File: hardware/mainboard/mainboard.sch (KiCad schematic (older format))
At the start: 3 parts, among them J1 top header, J4 bottom header, J5 almost bottom header

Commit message: First pass layout & component selection for mainboard
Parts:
- removed J1: top header, MF_Connectors:MF_Connectors-PTH_2.54MM_01X14, symbol Connector_Generic:Conn_01x14
- added MH1: M3, MountingHole:MountingHole_3.2mm_M3_Pad_Via, symbol Mechanical:MountingHole_Pad
- J4: value bottom header -> left header; footprint MF_Connectors:MF_Connectors-PTH_2.54MM_01X24 -> Connector_PinHeader_2.54mm:PinHeader_1x20_P2.54mm_Vertical; symbol Connector_Generic:Conn_01x24 -> Connector_Generic:Conn_01x20; finalized (none) -> yes; mpn (none) -> MF-CON-2.54mm-01x20
- J5: value almost bottom header -> right header; footprint MF_Connectors:MF_Connectors-PTH_2.54MM_01X14 -> Connector_PinHeader_2.54mm:PinHeader_1x20_P2.54mm_Vertical; symbol Connector_Generic:Conn_01x14 -> Connector_Generic:Conn_01x20; finalized (none) -> yes; mpn (none) -> MF-CON-2.54mm-01x20
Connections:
- net +12v-raw: now also J5.18 (Pin_18), J5.19 (Pin_19)
- net +3.3VA: now also J4.17 (Pin_17)
- net +3V3: now also J5.17 (Pin_17)
- net -12v-raw: now also J4.18 (Pin_18), J4.19 (Pin_19)
- net GND: now also J4.20 (Pin_20), J5.1 (Pin_1), J5.20 (Pin_20), MH1.1; no longer J4.12 (Pin_12), J4.13 (Pin_13), J4.24 (Pin_24), J5.7 (Pin_7), J5.8 (Pin_8)
- net castor_mix_out: now also J4.3 (Pin_3); no longer J5.12 (Pin_12)
- net castor_pwm_mix_in: now also J4.5 (Pin_5); no longer J4.20 (Pin_20)
- net castor_pwm_out: now also J4.8 (Pin_8); no longer J5.13 (Pin_13)
- net castor_ramp_mix_in: now also J4.6 (Pin_6); no longer J4.21 (Pin_21)
- net castor_ramp_out: now also J4.9 (Pin_9); no longer J4.23 (Pin_23)
- net castor_sub_mix_in: now also J4.4 (Pin_4); no longer J5.14 (Pin_14)
- net castor_sub_out: now also J4.7 (Pin_7); no longer J4.22 (Pin_22)
- net cv_a_jack: now also J5.8 (Pin_8); no longer J5.1 (Pin_1)
- net cv_a_pot: now also J5.14 (Pin_14); no longer J5.3 (Pin_3)
- net cv_b_jack: now also J5.7 (Pin_7); no longer J5.2 (Pin_2)
- net cv_b_pot: now also J5.13 (Pin_13); no longer J4.8 (Pin_8)
- net dotstar_clk: now also J5.16 (Pin_16)
- net dotstar_data: now also J5.15 (Pin_15)
- net duty_a_jack: now also J5.5 (Pin_5); no longer J4.2 (Pin_2)
- net duty_a_pot: now also J5.11 (Pin_11); no longer J4.7 (Pin_7)
- net duty_b_jack: now also J5.9 (Pin_9); no longer J4.3 (Pin_3)
- net duty_b_pot: now also J5.10 (Pin_10); no longer J4.5 (Pin_5)
- net mix_out: now also J5.2 (Pin_2); no longer J5.5 (Pin_5)
- net mix_pot_in: now also J5.3 (Pin_3); no longer J5.4 (Pin_4)
- net mix_pot_out: now also J5.4 (Pin_4); no longer J5.6 (Pin_6)
- net phase_jack: now also J5.6 (Pin_6); no longer J4.4 (Pin_4)
- net phase_pot: now also J5.12 (Pin_12); no longer J4.6 (Pin_6)
- net pollux_mix_out: now also J4.10 (Pin_10); no longer J5.10 (Pin_10)
- net pollux_pwm_mix_in: now also J4.12 (Pin_12); no longer J4.16 (Pin_16)
- net pollux_pwm_out: now also J4.15 (Pin_15); no longer J5.9 (Pin_9)
- net pollux_ramp_mix_in: now also J4.13 (Pin_13); no longer J4.17 (Pin_17)
- net pollux_ramp_out: now also J4.16 (Pin_16); no longer J4.19 (Pin_19)
- net pollux_sub_mix_in: now also J4.11 (Pin_11); no longer J5.11 (Pin_11)
- net pollux_sub_out: now also J4.14 (Pin_14); no longer J4.18 (Pin_18)

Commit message: Fixup ERC errors
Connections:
- net GND: now also J4.2 (Pin_2)
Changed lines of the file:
@@
 	1    0    0    -1
 $EndComp
+$Comp
+L power:GND #PWR0141
+U 1 1 5F22906B
+P 2200 7550
+F 0 "#PWR0141" H 2200 7300 50  0001 C CNN
+F 1 "GND" V 2200 7350 50  0000 C CNN
+F 2 "" H 2200 7550 50  0001 C CNN
+F 3 "" H 2200 7550 50  0001 C CNN
+	1    2200 7550
+	0    1    -1   0
+$EndComp
 $EndSCHEMATC

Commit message: Bumb schematics after generating gerbers and assigning alt mpns
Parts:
- J4, J5: mpn alt (none) -> 929974-01-20-RK
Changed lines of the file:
@@
 F 4 "yes" H 2400 6750 50  0001 C CNN "finalized"
 F 5 "MF-CON-2.54mm-01x20" H 2400 6750 50  0001 C CNN "mpn"
+F 6 "929974-01-20-RK" H 2400 6750 50  0001 C CNN "mpn alt"
 	1    2400 6750
 	1    0    0    1
@@
 F 4 "yes" H 3100 6750 50  0001 C CNN "finalized"
 F 5 "MF-CON-2.54mm-01x20" H 3100 6750 50  0001 C CNN "mpn"
+F 6 "929974-01-20-RK" H 3100 6750 50  0001 C CNN "mpn alt"
 	1    3100 6750
 	-1   0    0    1

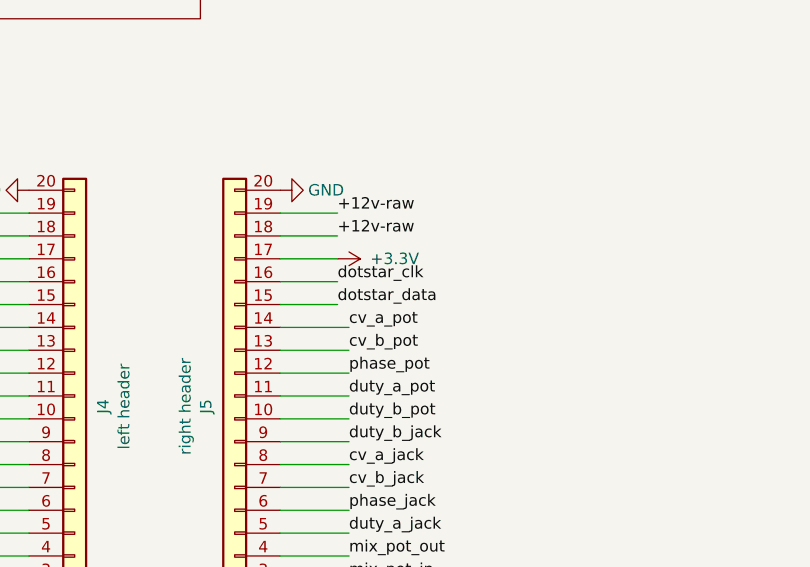
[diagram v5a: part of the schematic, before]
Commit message: Swap dotstar clk and data on mainboard (label only change, no hardware change)
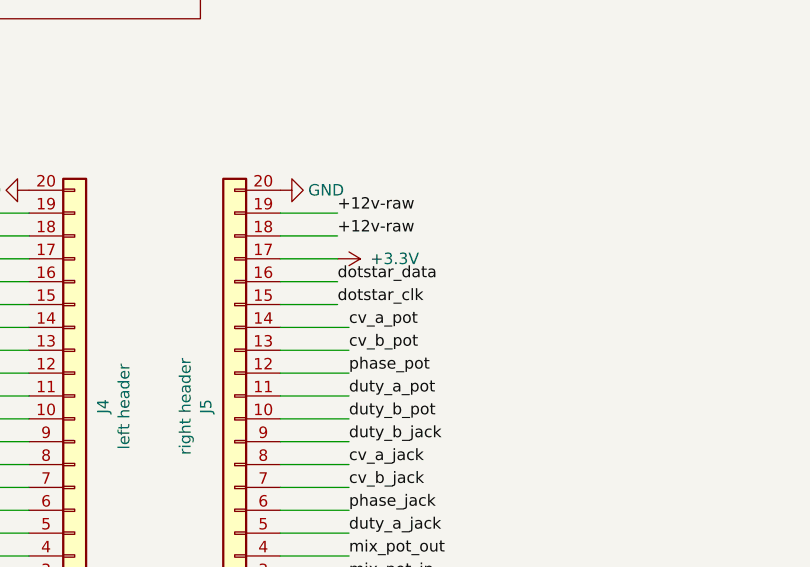
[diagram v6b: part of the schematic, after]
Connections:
- net dotstar_clk: now also J5.15 (Pin_15); no longer J5.16 (Pin_16)
- net dotstar_data: now also J5.16 (Pin_16); no longer J5.15 (Pin_15)
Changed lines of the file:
@@
 Wire Wire Line
 	2800 950  3050 950
+Text Label 3550 6150 0    50   ~ 0
+dotstar_data
 Text Label 3550 6250 0    50   ~ 0
-dotstar_data
-Text Label 3550 6150 0    50   ~ 0
 dotstar_clk
 $Comp

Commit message: Double check MPNs
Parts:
- J4, J5: mpn MF-CON-2.54mm-01x20 -> 4UCON 21790; mpn alt 929974-01-20-RK -> (none)
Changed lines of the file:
@@
 F 3 "~" H 2400 6750 50  0001 C CNN
 F 4 "yes" H 2400 6750 50  0001 C CNN "finalized"
-F 5 "MF-CON-2.54mm-01x20" H 2400 6750 50  0001 C CNN "mpn"
-F 6 "929974-01-20-RK" H 2400 6750 50  0001 C CNN "mpn alt"
+F 5 "4UCON 21790" H 2400 6750 50  0001 C CNN "mpn"
+F 6 "" H 2400 6750 50  0001 C CNN "mpn alt"
 	1    2400 6750
 	1    0    0    1
@@
 F 3 "~" H 3100 6750 50  0001 C CNN
 F 4 "yes" H 3100 6750 50  0001 C CNN "finalized"
-F 5 "MF-CON-2.54mm-01x20" H 3100 6750 50  0001 C CNN "mpn"
-F 6 "929974-01-20-RK" H 3100 6750 50  0001 C CNN "mpn alt"
+F 5 "4UCON 21790" H 3100 6750 50  0001 C CNN "mpn"
+F 6 "" H 3100 6750 50  0001 C CNN "mpn alt"
 	1    3100 6750
 	-1   0    0    1

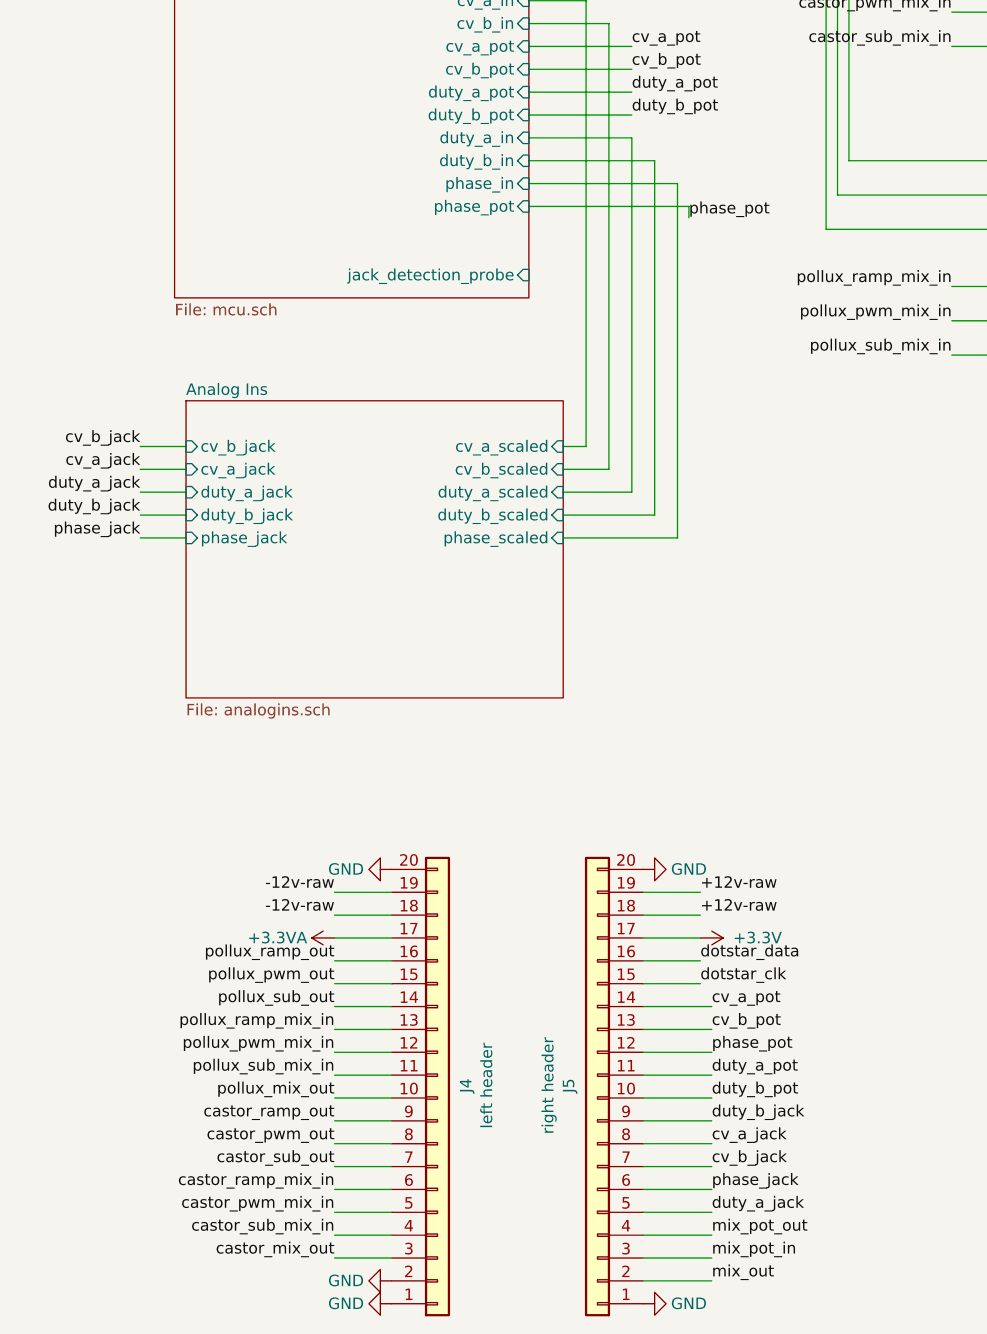
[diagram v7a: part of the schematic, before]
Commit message: Change phase in to hard sync button, remove unneeded parts, make v2 mainboard
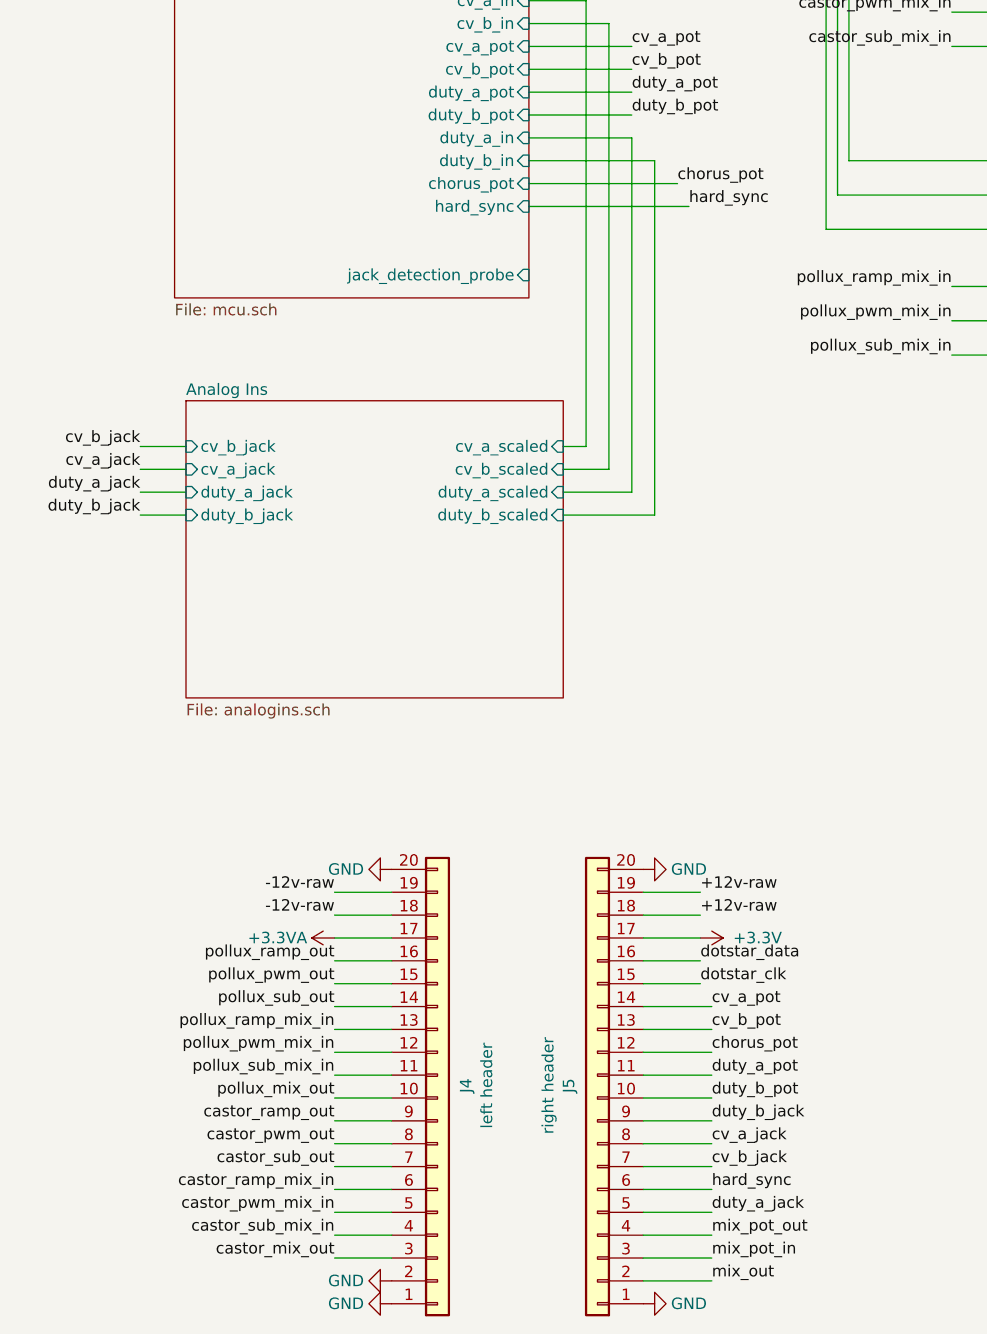
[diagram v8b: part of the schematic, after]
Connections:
- net phase_jack renamed hard_sync
- net phase_pot renamed chorus_pot
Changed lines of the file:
@@
 Sheet 1 7
 Title "Castor & Pollux"
-Date "2020-09-07"
-Rev "v1"
+Date "2020-09-26"
+Rev "v2"
 Comp "Winterbloom"
 Comment1 "CC BY-SA 4.0"
@@
 F8 "duty_b_scaled" I R 2950 4200 50
 F9 "duty_b_jack" I L 1300 4200 50
-F10 "phase_jack" I L 1300 4300 50
-F11 "phase_scaled" I R 2950 4300 50
 $EndSheet
 Wire Wire Line
@@
 Wire Wire Line
 	3350 2650 2800 2650
-Wire Wire Line
-	2950 4300 3450 4300
-Wire Wire Line
-	3450 4300 3450 2750
 Wire Wire Line
 	3450 2750 2800 2750
@@
 F16 "duty_a_in" I R 2800 2550 50
 F17 "duty_b_in" I R 2800 2650 50
-F18 "phase_in" I R 2800 2750 50
-F19 "phase_pot" I R 2800 2850 50
 F20 "jack_detection_probe" I R 2800 3150 50
+F21 "hard_sync" I R 2800 2850 50
+F22 "chorus_pot" I R 2800 2750 50
 $EndSheet
 $Sheet
@@
 Text Label 1100 4200 2    50   ~ 0
 duty_b_jack
-Text Label 1100 4300 2    50   ~ 0
-phase_jack
 Wire Wire Line
 	1100 3900 1300 3900
@@
 Wire Wire Line
 	1100 4200 1300 4200
-Wire Wire Line
-	1100 4300 1300 4300
 Text Label 3250 2150 0    50   ~ 0
 cv_a_pot
@@
 Text Label 3250 2450 0    50   ~ 0
 duty_b_pot
-Text Label 3500 2900 0    50   ~ 0
-phase_pot
 Wire Wire Line
 	3250 2150 2800 2150
@@
 Wire Wire Line
 	2800 2850 3500 2850
-Wire Wire Line
-	3500 2850 3500 2900
 Text Label 4650 1850 2    50   ~ 0
 castor_ramp_mix_in
@@
 	3600 7150 3300 7150
 Text Label 3600 7150 0    50   ~ 0
-phase_jack
+hard_sync
 Text Label 3600 6850 0    50   ~ 0
 duty_b_jack
@@
 duty_a_jack
 Text Label 3600 6550 0    50   ~ 0
-phase_pot
+chorus_pot
 Text Label 3600 6750 0    50   ~ 0
 duty_b_pot
@@
 	0    1    -1   0
 $EndComp
+Text Label 3450 2750 0    50   ~ 0
+chorus_pot
+Text Label 3500 2850 0    50   ~ 0
+hard_sync
 $EndSCHEMATC
